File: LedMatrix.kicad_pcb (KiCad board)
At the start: 2 copper layers, 28 parts, among them IC1 ATMEGA328P-A, P1 FTDI, P2 SYNC_OUT, P3 ICSP, SW1 SW_PUSH, SW2 SWITCH_INV, U1 74HC238, U2 M54562FP, U3 MCP1700-3302, U4 TLC5917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

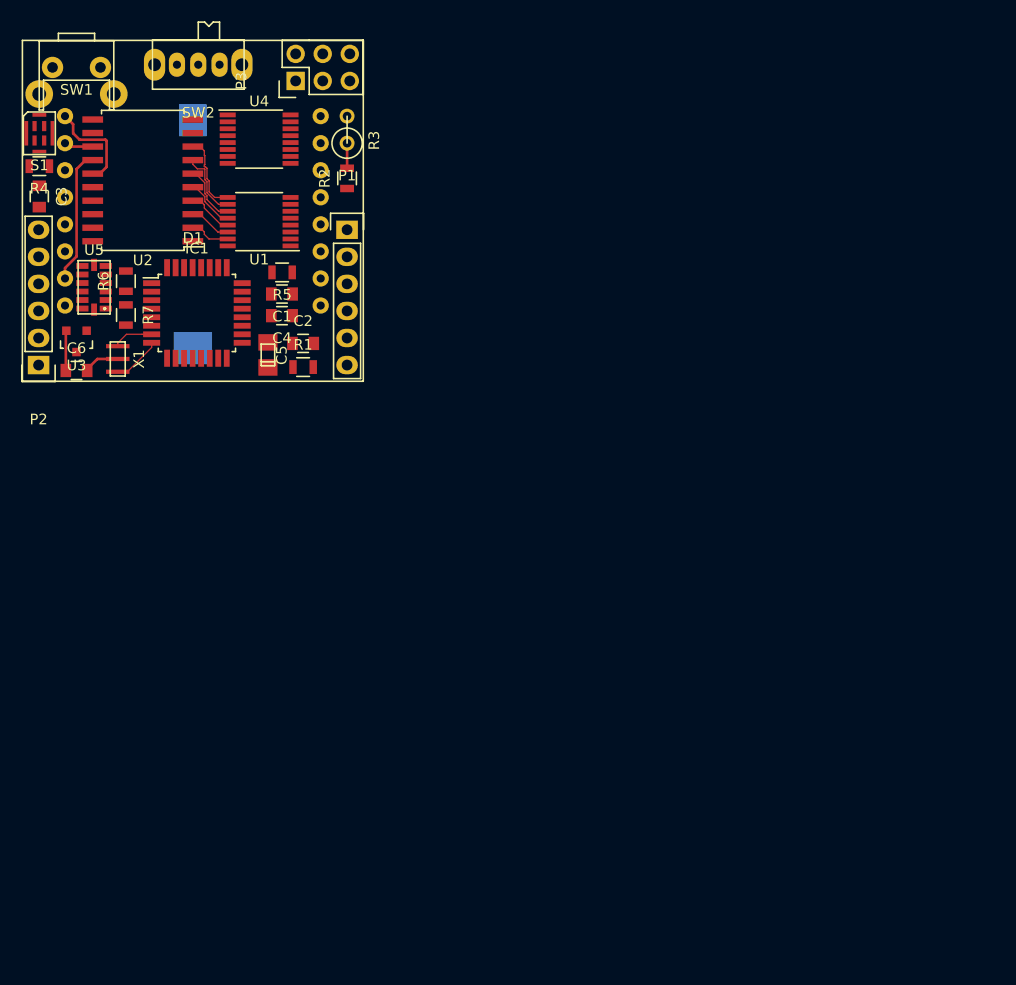
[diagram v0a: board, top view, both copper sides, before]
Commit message: Update the LED control program
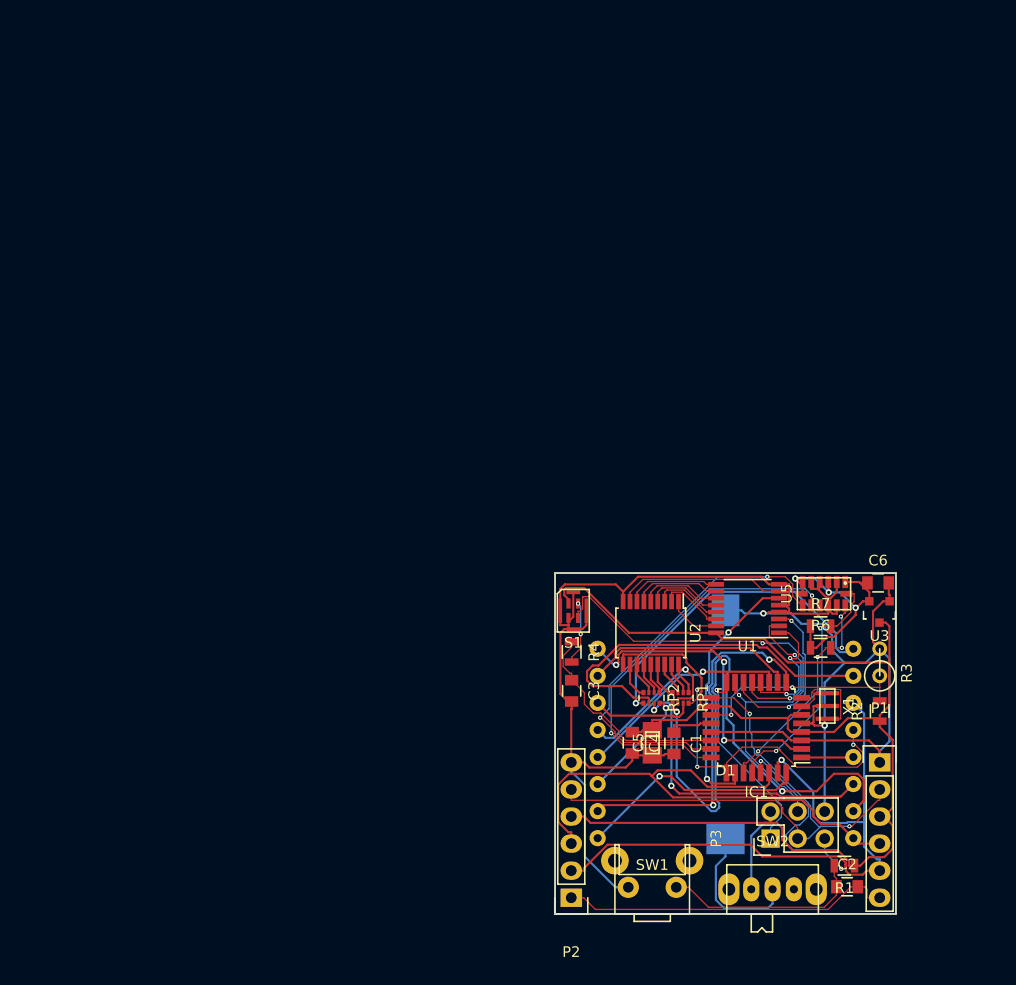
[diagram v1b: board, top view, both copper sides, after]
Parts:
- removed R5: R, Resistors_SMD:R_0805
- removed U4: TLC5917, Housings_SSOP:TSSOP-16_4.4x5mm_Pitch0.65mm
- added RP1: R_PACK4, Resistors_SMD:R_Array_Convex_4x0402, F.Cu at (45.8, 45.7)
- added RP2: R_PACK4, Resistors_SMD:R_Array_Convex_4x0402, F.Cu at (43.1, 45.7)
- U2: value M54562FP -> TD62083AFNG; footprint Housings_SOIC:SOIC-20_7.5x12.8mm_Pitch1.27mm -> SSOP18:TSSOP-14_4.4x5mm_Pitch0.65mm
- moved SW2 94.3 mm to (54.4, 63.7), turned to 0 degrees
- moved SW1 94.0 mm to (43.1, 63.5), turned to 0 degrees
- moved P3 83.9 mm to (54.2, 58.9)
- moved U3 79.5 mm to (64.5, 37.7)
- moved C6 77.8 mm to (64.3, 34.9)
- moved U5 74.3 mm to (59.2, 35.9), turned to 270 degrees
- moved X1 74.2 mm to (59.6, 46.5)
- moved R6 73.7 mm to (58.9, 41.0), turned to 0 degrees
- moved C2 72.2 mm to (61.4, 63.4)
- moved R7 71.5 mm to (58.9, 39.0), turned to 0 degrees
- moved D1 70.7 mm to (50.0, 50.0)
- moved P1 70.7 mm to (64.5, 51.8)
- moved P2 70.7 mm to (35.5, 64.5)
- moved R2 70.7 mm to (64.5, 47.0)
- moved R3 70.7 mm to (64.5, 42.4)
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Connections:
- D1 pad 1: Net-(D1-Pad1) -> /ROW5
- D1 pad 12: Net-(D1-Pad12) -> /ROW4
- D1 pad 14: Net-(D1-Pad14) -> /ROW2
- D1 pad 2: Net-(D1-Pad2) -> /ROW7
- D1 pad 5: Net-(D1-Pad5) -> /ROW8
- D1 pad 7: Net-(D1-Pad7) -> /ROW6
- D1 pad 8: Net-(D1-Pad8) -> /ROW3
- D1 pad 9: Net-(D1-Pad9) -> /ROW1
- IC1 pad 1: /ADXL345_INT2 -> /ROW4
- IC1 pad 10: (no net) -> /ROW7
- IC1 pad 11: Net-(IC1-Pad11) -> /ROW8
- IC1 pad 15: /MOSI -> /AUDIO_CLK
- IC1 pad 17: /SCK -> /RTS
- IC1 pad 19: (no net) -> /LIGHT_SENSE
- IC1 pad 2: /TLC5917_OE -> /ROW5
- IC1 pad 22: (no net) -> /AUDIO_IN
- IC1 pad 23: /LIGHT_SENSE -> /ADXL345_INT1
- IC1 pad 24: /AUDIO_IN -> /ADXL345_INT2
- IC1 pad 26: (no net) -> /LOWSIDE_EN
- IC1 pad 30: /RXI -> /ROW1
- IC1 pad 31: /TXO -> /ROW2
- IC1 pad 32: /ADXL345_INT1 -> /ROW3
- IC1 pad 9: /AUDIO_CLK -> /ROW6
- P1 pad 2: GND -> /RTS
- P1 pad 4: /RXI -> /ROW1
- P1 pad 5: /TXO -> /ROW2
- P2 pad 2: /TXO -> /ROW2
- P2 pad 3: /RXI -> /ROW1
- P2 pad 5: GND -> /RTS
- P3 pad 3: /SCK -> /RTS
- P3 pad 4: /MOSI -> /AUDIO_CLK
- SW2 pad 3: (no net) -> Net-(SW2-Pad3)
- U1 pad 6: Net-(IC1-Pad11) -> /LOWSIDE_EN
- U2 pad 1: (no net) -> Net-(U1-Pad15)
- U2 pad 11: GND -> Net-(RP2-Pad4)
- U2 pad 12: Net-(D1-Pad5) -> Net-(RP2-Pad3)
- U2 pad 13: Net-(D1-Pad2) -> Net-(RP2-Pad2)
- U2 pad 14: Net-(D1-Pad7) -> Net-(RP2-Pad1)
- U2 pad 15: Net-(D1-Pad1) -> Net-(RP1-Pad4)
- U2 pad 16: Net-(D1-Pad12) -> Net-(RP1-Pad3)
- U2 pad 17: Net-(D1-Pad8) -> Net-(RP1-Pad2)
- U2 pad 18: Net-(D1-Pad14) -> Net-(RP1-Pad1)
- U2 pad 2: Net-(U1-Pad15) -> Net-(U1-Pad14)
- U2 pad 3: Net-(U1-Pad14) -> Net-(U1-Pad13)
- U2 pad 4: Net-(U1-Pad13) -> Net-(U1-Pad12)
- U2 pad 5: Net-(U1-Pad12) -> Net-(U1-Pad11)
- U2 pad 6: Net-(U1-Pad11) -> Net-(U1-Pad10)
- U2 pad 7: Net-(U1-Pad10) -> Net-(U1-Pad9)
- U2 pad 8: Net-(U1-Pad9) -> Net-(U1-Pad7)
- U2 pad 9: Net-(U1-Pad7) -> GND
- U5 pad 1: (no net) -> /3v3
- U5 pad 10: (no net) -> Net-(U5-Pad10)
- U5 pad 6: (no net) -> /3v3
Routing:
- net GND: track 3.39 -> 167.6 mm, vias 0 -> 2
- net VCC: track 0.00 -> 142.5 mm
- net /ROW2: track 0.00 -> 61.9 mm, vias 0 -> 1
- net Net-(D1-Pad10): track 0.00 -> 54.8 mm, vias 0 -> 2
- net /ROW1: track 0.00 -> 52.8 mm
- net /RTS: track 0.00 -> 52.7 mm, vias 0 -> 2
- net /AUDIO_CLK: track 0.00 -> 49.1 mm, vias 0 -> 2
- net /ADXL345_INT1: track 0.00 -> 39.3 mm, vias 0 -> 2
- net /RESET: track 0.00 -> 39.2 mm, vias 0 -> 2
- net /ADXL345_INT2: track 0.00 -> 38.5 mm, vias 0 -> 2
- net Net-(D1-Pad15): track 0.00 -> 35.0 mm
- net /ROW6: track 0.00 -> 33.9 mm, vias 0 -> 2
- net /DTR: track 0.00 -> 31.2 mm
- net /LED_SENSE: track 0.00 -> 30.8 mm, vias 0 -> 3
- net Net-(D1-Pad16): track 0.00 -> 30.8 mm, vias 0 -> 1
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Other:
- board outline added: 32 x 32 mm
- net class Default: clearance 0.2 -> 0.1; trace_width 0.25 -> 0.2
- net class PR added: clearance 0.1, trace_width 0.2, via_dia 0.6, via_drill 0.4
- rule trace_clearance: 0.2 -> 0.1

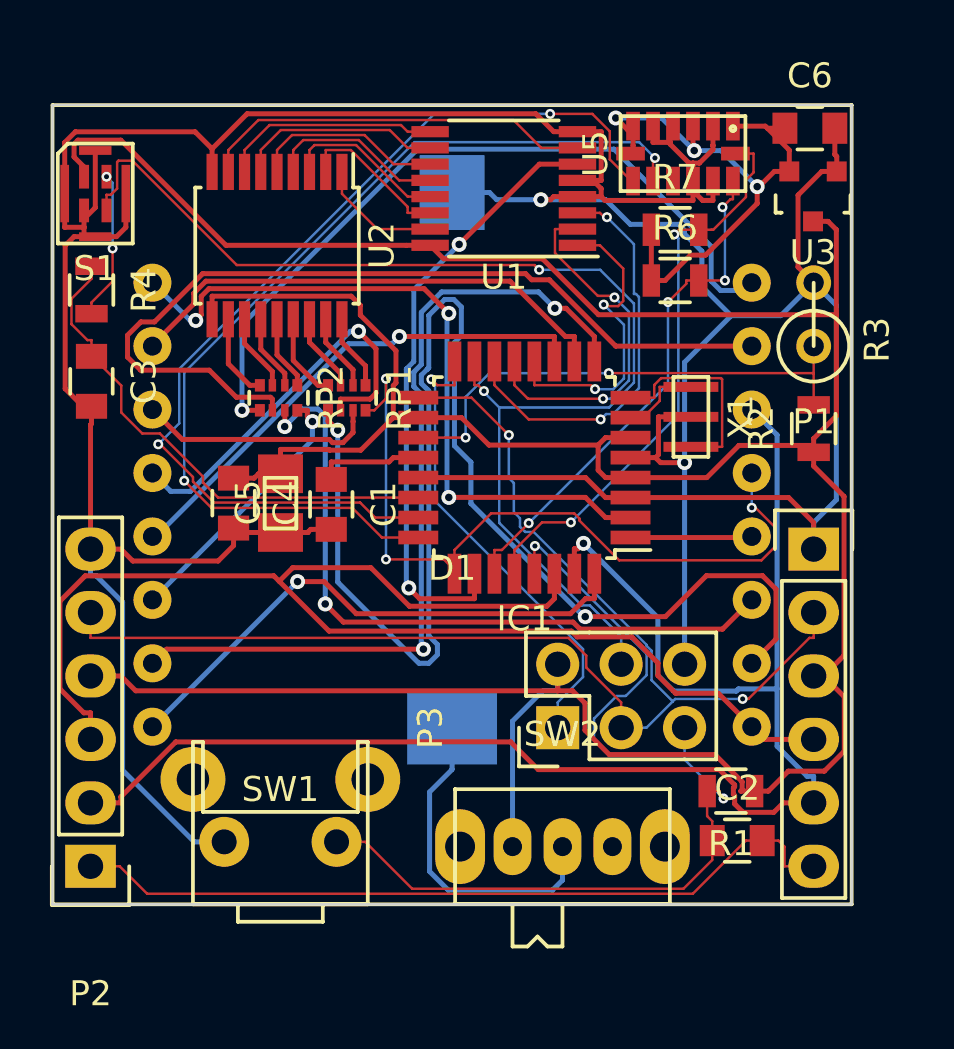
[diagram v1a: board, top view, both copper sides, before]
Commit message: Use flash memory for animation
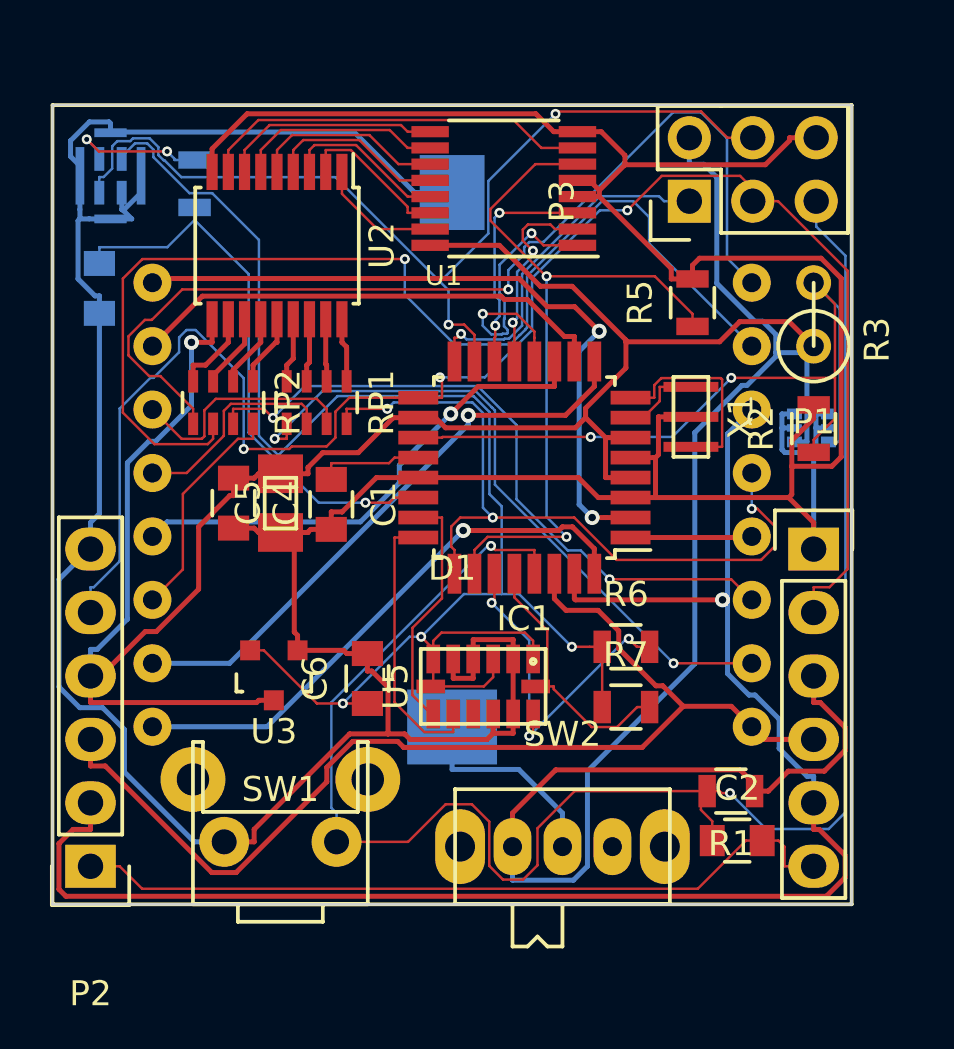
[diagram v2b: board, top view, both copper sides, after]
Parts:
- added R5: 10k, Resistors_SMD:R_0805, F.Cu at (59.6, 41.9)
- added U4: PNJ4K01F, pnj4k01f:KPTFTN6K0001, B.Cu at (64.4, 46.9)
- C3: value C -> 10nf; moved to B.Cu
- C4: value C -> 0.1uf
- C5: value CP -> 10uf
- R1: value R -> 10k
- R2: value R -> 100k
- R4: value R -> 10k; moved to B.Cu
- R6, R7: value R -> 2k
- RP1, RP2: footprint Resistors_SMD:R_Array_Convex_4x0402 -> Resistors_SMD:R_Array_Concave_4x0603
- S1: moved to B.Cu
- moved U3 28.9 mm to (42.9, 56.8)
- moved C6 28.3 mm to (46.6, 57.0), turned to 90 degrees
- moved U5 22.8 mm to (51.2, 57.3)
- moved P3 21.7 mm to (59.5, 37.8)
- moved R7 19.2 mm to (57.0, 58.1)
- moved R6 14.8 mm to (57.0, 55.7)
- moved R4 5.93 mm to (39.7, 37.1), turned to 90 degrees
- moved C3 3.73 mm to (35.9, 41.3)
- moved RP2 2.23 mm to (40.8, 45.9)
- moved RP1 1.22 mm to (44.6, 45.9)
- moved S1 0.94 mm to (36.3, 36.8), turned to 180 degrees
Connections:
- R2 pad 1: VCC -> /LIGHT_SENSE
- R2 pad 2: /LIGHT_SENSE -> GND
- R3 pad 1: /LIGHT_SENSE -> VCC
- R3 pad 2: GND -> /LIGHT_SENSE
- S1 pad 1: VCC -> /3v3
- SW2 pad 3: Net-(SW2-Pad3) -> (no net)
- U5 pad 10: Net-(U5-Pad10) -> (no net)
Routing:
- net /3v3: track 23.8 -> 65.7 mm
- net /RESET: track 39.2 -> 71.1 mm
- net /ADXL345_INT1: track 39.3 -> 9.69 mm, vias 2 -> 0
- net Net-(D1-Pad10): track 54.8 -> 27.2 mm
- net /ADXL345_INT2: track 38.5 -> 11.1 mm, vias 2 -> 0
- net GND: track 167.6 -> 188.6 mm, vias 2 -> 0
- net /RTS: track 52.7 -> 66.8 mm, vias 2 -> 3
- net /SCL: track 23.1 -> 10.7 mm, vias 2 -> 0
- net /LIGHT_SENSE: track 20.2 -> 32.4 mm
- net /ROW6: track 33.9 -> 23.5 mm, vias 2 -> 1
- net /AUDIO_CLK: track 49.1 -> 39.1 mm
- net Net-(D1-Pad15): track 35.0 -> 44.6 mm, vias 0 -> 1
- net Net-(D1-Pad16): track 30.8 -> 39.8 mm
- net /ROW1: track 52.8 -> 44.0 mm
- net Net-(D1-Pad4): track 15.9 -> 8.59 mm, vias 1 -> 0
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
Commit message: Brightness code
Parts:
- P3, SW1, SW2: moved to B.Cu
- moved P3 4.89 mm to (64.4, 37.8)
- turned SW1 to 180 degrees
- turned SW2 to 180 degrees
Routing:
- net GND: track 188.6 -> 149.9 mm, vias 0 -> 3
- net /ROW2: track 65.0 -> 49.6 mm
- net VCC: track 143.3 -> 132.1 mm, vias 1 -> 3
- net Net-(D1-Pad15): track 44.6 -> 33.6 mm
- net /RESET: track 71.1 -> 60.2 mm, vias 2 -> 3
- net /SCL: track 10.7 -> 20.4 mm, vias 0 -> 3
- net /ROW1: track 44.0 -> 52.5 mm
- net /ROW8: track 20.0 -> 26.5 mm
- net Net-(D1-Pad6): track 9.07 -> 15.5 mm
- net /ROW5: track 28.4 -> 23.1 mm, vias 2 -> 1
- net /MISO: track 14.2 -> 19.4 mm
- net Net-(IC1-Pad12): track 11.9 -> 7.14 mm
- net /LOWSIDE_EN: track 30.5 -> 25.8 mm
- net Net-(IC1-Pad8): track 8.26 -> 12.7 mm, vias 0 -> 2
- net Net-(D1-Pad16): track 39.8 -> 43.9 mm, vias 1 -> 0
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- added copper zone on B.Cu, net GND
- added copper zone on F.Cu, net GND
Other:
- net class SIGNAL: via_dia 0.4 -> 0.5; via_drill 0.2 -> 0.3
- board text added: "DotDotLab"
- board text added: "EdwardRF Mika Lin"

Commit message: Add francis and northy mods
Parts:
- removed S1: MP34DT01, MP34DT01:MP34DT01
- removed SW2: SWITCH_INV, 1P2T:1P2T_SideSwitch
- added C7: 1uf, Capacitors_SMD:C_0603, F.Cu at (47.2, 63.8)
- added D2: D_Schottky, Diodes_SMD:SMA_Standard, B.Cu at (54.9, 62.8)
- added M1: 3729Mic, 3729Mic:3729Mic, B.Cu at (36.6, 37.1)
- added P0: CONN_01X04, Pin_Headers:Pin_Header_Straight_1x04, B.Cu at (64.8, 57.0)
- added R8: 100k, Resistors_SMD:R_0603, F.Cu at (39.9, 59.6)
- added R9: 10k, Resistors_SMD:R_0603, F.Cu at (37.0, 60.9)
- added U6: APDS-9900, ADPS-9900:ADPS-9900, B.Cu at (64.4, 49.7)
- added U7: AP1117D30, TO_SOT_Packages_SMD:SOT-223, B.Cu at (42.8, 62.4)
- added X2: 12Mhz, CSTCE8M:CSTCE8M00G52, F.Cu at (49.3, 57.8)
- C1, C2, C4, C6: footprint Capacitors_SMD:C_0805 -> Capacitors_SMD:C_0603
- C3: value 10nf -> 0.1uf; footprint Capacitors_SMD:C_0805 -> Capacitors_SMD:C_0603; moved to F.Cu
- IC1: footprint Housings_QFP:TQFP-32_7x7mm_Pitch0.8mm -> Housings_DFN_QFN:QFN-32-1EP_5x5mm_Pitch0.5mm
- P1: value FTDI -> CONN_01X04; footprint Pin_Headers:Pin_Header_Straight_1x06 -> Pin_Headers:Pin_Header_Straight_1x04; moved to B.Cu
- P2: value SYNC_OUT -> USB_OTG; footprint Pin_Headers:Pin_Header_Straight_1x06 -> Molex475890001:47589-0001
- R1, R2, R5, R6, R7: footprint Resistors_SMD:R_0805 -> Resistors_SMD:R_0603
- R3: value Photores -> 100k; footprint Discret:R1 -> Resistors_SMD:R_0603
- R4: footprint Resistors_SMD:R_0805 -> Resistors_SMD:R_0603; moved to F.Cu
- SW1: footprint SideButton:SidePushButton -> SKSCLCE010:SKSCLCE010; moved to F.Cu
- U3: value MCP1700-3302 -> CH340T; footprint Housings_SOT-23_SOT-143_TSOT-6:SOT-23 -> Housings_SSOP:SSOP-20_5.3x7.2mm_Pitch0.65mm
- U4: value PNJ4K01F -> TPCP8405; footprint pnj4k01f:KPTFTN6K0001 -> ps_8:PS-8; moved to F.Cu
- moved P1 29.7 mm to (35.2, 57.0), turned to 180 degrees
- moved R4 25.7 mm to (43.2, 62.6), turned to 0 degrees
- moved U4 25.0 mm to (42.9, 59.8)
- moved P2 19.4 mm to (54.9, 63.1), turned to 0 degrees
- moved R6 13.8 mm to (43.2, 55.4)
- moved U3 12.7 mm to (55.5, 55.1), turned to 0 degrees
- moved R7 11.0 mm to (46.4, 55.4)
- moved C4 9.77 mm to (50.3, 46.2)
- moved U5 6.87 mm to (46.4, 52.5)
- moved R2 6.83 mm to (64.5, 53.8)
- moved C5 6.23 mm to (48.1, 46.2)
- moved C6 6.16 mm to (42.5, 52.3)
- moved SW1 4.03 mm to (39.1, 63.9), turned to 0 degrees
- moved C1 3.58 mm to (48.6, 49.1), turned to 180 degrees
- moved R3 3.23 mm to (64.5, 45.6), turned to 270 degrees
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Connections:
- C2 pad 2: /DTR -> Net-(C2-Pad2)
- C3 pad 1: /AUDIO_IN -> GND
- C3 pad 2: GND -> Net-(C3-Pad2)
- C4 pad 1: VCC -> Net-(BT1-Pad1)
- C5 pad 1: VCC -> Net-(BT1-Pad1)
- C6 pad 1: /3v3 -> Net-(C6-Pad1)
- IC1 pad 15: /AUDIO_CLK -> /MOSI
- IC1 pad 17: /RTS -> /SCK
- IC1 pad 19: /LIGHT_SENSE -> /LED_SENSE
- IC1 pad 25: /LED_SENSE -> /LIGHT_INT
- P1 pad 1: GND -> VCC
- P1 pad 2: /RTS -> /MOSI
- P1 pad 3: VCC -> /SCK
- P1 pad 4: /ROW1 -> GND
- P2 pad 1: /DTR -> /5V
- P2 pad 2: /ROW2 -> /D-
- P2 pad 3: /ROW1 -> /D+
- P2 pad 4: VCC -> (no net)
- P2 pad 5: /RTS -> GND
- P2 pad 6: GND -> Net-(P2-Pad6)
- P3 pad 3: /RTS -> /SCK
- P3 pad 4: /AUDIO_CLK -> /MOSI
- R2 pad 1: /LIGHT_SENSE -> /ROW1
- R2 pad 2: GND -> Net-(R2-Pad2)
- R3 pad 1: VCC -> /ROW2
- R3 pad 2: /LIGHT_SENSE -> Net-(R3-Pad2)
- R4 pad 1: /AUDIO_IN -> Net-(BT1-Pad1)
- R6 pad 1: /3v3 -> VCC
- R7 pad 1: /3v3 -> VCC
- SW1 pad 1: GND -> Net-(C7-Pad1)
- SW1 pad 2: /RESET -> Net-(R9-Pad2)
- U3 pad 1: GND -> (no net)
- U3 pad 2: /3v3 -> (no net)
- U3 pad 3: VCC -> Net-(R2-Pad2)
- U4 pad 1: VCC -> GND
- U4 pad 2: GND -> Net-(R9-Pad2)
- U4 pad 3: GND -> Net-(BT1-Pad1)
- U4 pad 4: GND -> Net-(R4-Pad2)
- U4 pad 5: GND -> VCC
- U4 pad 6: /LIGHT_SENSE -> VCC
- U5 pad 1: /3v3 -> VCC
- U5 pad 3: /3v3 -> VCC
- U5 pad 6: /3v3 -> VCC
- U5 pad 7: /3v3 -> VCC
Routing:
- net GND: track 149.9 -> 228.7 mm, vias 3 -> 4
- net /3v3: track 67.3 -> 0.00 mm, vias 2 -> 0
- net /SCK: track 0.00 -> 64.7 mm, vias 0 -> 2
- net /RTS: track 63.4 -> 0.00 mm, vias 1 -> 0
- net /MOSI: track 0.00 -> 45.5 mm, vias 0 -> 2
- net VCC: track 132.1 -> 170.0 mm, vias 3 -> 6
- net /AUDIO_CLK: track 35.8 -> 0.00 mm, vias 1 -> 0
- net /ROW1: track 52.5 -> 18.3 mm, vias 0 -> 2
- net /LIGHT_SENSE: track 33.8 -> 0.00 mm, vias 1 -> 0
- net /DTR: track 31.2 -> 0.00 mm
- net /ROW2: track 49.6 -> 19.9 mm
- net Net-(C3-Pad2): track 0.00 -> 29.0 mm
- net Net-(C6-Pad1): track 0.00 -> 28.7 mm, vias 0 -> 1
- net /RESET: track 60.2 -> 32.4 mm, vias 3 -> 2
- net Net-(R3-Pad2): track 0.00 -> 25.2 mm, vias 0 -> 2
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- removed copper zone on B.Cu, net GND
- removed copper zone on F.Cu, net GND
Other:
- outline, holes or cut-outs redrawn
- board text added: "1"
- board text added: "16"
- board text added: "G"
- board text added: "Gnd"
- board text added: "ICSP"
- board text added: "Miso"
- board text added: "Mosi"
- board text added: "PWR"
- board text added: "Sck"
- board text added: "Vcc"
- board text added: "isobar"
- board text added: "nowlab"
- board text removed: "DotDotLab"
- board text removed: "EdwardRF Mika Lin"
